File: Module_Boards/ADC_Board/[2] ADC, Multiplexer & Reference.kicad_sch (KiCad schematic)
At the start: 36 parts, among them J1 212134-0003, J2 212134-0003, J3 212134-0003, J4 212134-0003, U1 ADS8860IDRCT, U2 REF35250YBHR, U5 TMUX1104DQAR, U6 LTC6255IDC#TRMPBF, U7 OPA310SIDBVR, U8 OPA333AIDBVR

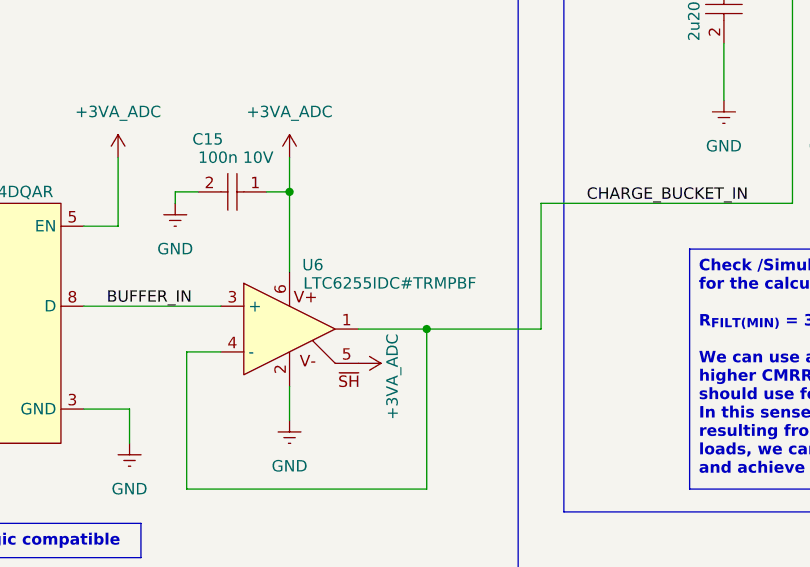
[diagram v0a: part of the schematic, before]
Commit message: A reference designator was not updated correctly.
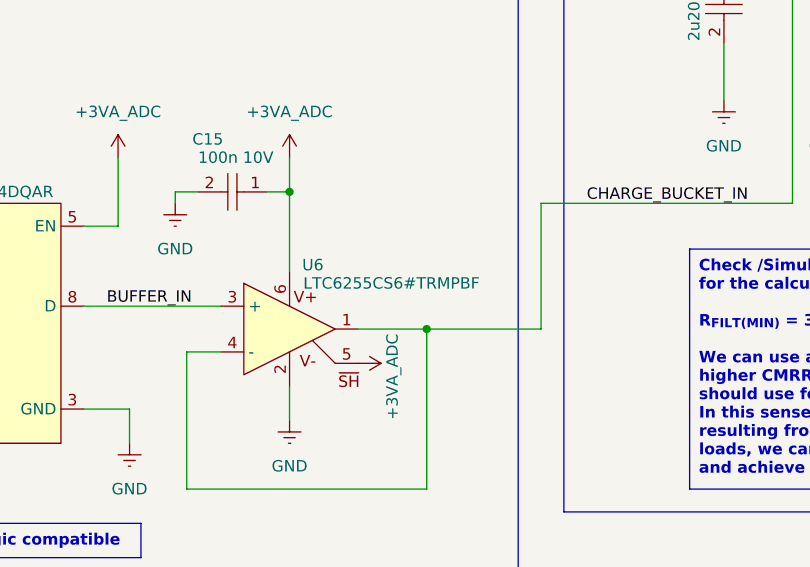
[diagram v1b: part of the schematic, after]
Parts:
- U6: value LTC6255IDC#TRMPBF -> LTC6255CS6#TRMPBF
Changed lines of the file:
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@@
 			)
 		)
-		(property "Value" "LTC6255IDC#TRMPBF"
+		(property "Value" "LTC6255CS6#TRMPBF"
 			(at 118.364 137.16 0)
 			(effects

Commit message: Push with updated readme
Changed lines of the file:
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@@
 		)
 	)
-	(text_box "Check /Simulations/ADC_Charge_Bucket/ADC_CHARGE_BUCKET.xlsx \nfor the calculation of the charge-bucket circuit components.\n\nR_{FILT(MIN)} = 322 Ω | R_{FILT(NOMINAL)} = 1286 Ω | R_{FILT(MAX)} = 2572 Ω | C_{FILT} = 180 pF\n\nWe can use a GND sense topology (balanced impedance in both INx paths) to achieve a \nhigher CMRR and cancel the offset error created by R_FILT. For this the value of R_{FILT} we\nshould use for both paths is R_{FILT}/2. However, the important aspect is the RC constant of the pair.\nIn this sense, a bigger resistor can result in a higher distortion (though it helps avoid the instability\nresulting from driving capacitive loads). In this case, as the driver buffer is designed to drive capacitive\nloads, we can increase the value of C_{FILT} (to 2.2 nF) and reduce the value of R_{FILT} (to 2*39 Ω = 78 Ω)\nand achieve better results (In simulations)"
+	(text_box "Check /Simulations/ADC_Charge_Bucket/ADC_CHARGE_BUCKET.xlsx \nfor the calculation of the charge-bucket circuit components.\n\nWe can use a GND sense topology (balanced impedance in both INx paths) to achieve a \nhigher CMRR and cancel the offset error created by R_FILT. For this the value of R_{FILT} we\nshould use for both paths is R_{FILT}/2. However, the important aspect is the RC constant of the pair.\nIn this sense, a bigger resistor can result in a higher distortion (though it helps avoid the instability\nresulting from driving capacitive loads). "
 		(exclude_from_sim no)
 		(at 161.29 133.35 0)
-		(size 109.22 26.67)
+		(size 109.22 19.05)
 		(stroke
 			(width 0)
